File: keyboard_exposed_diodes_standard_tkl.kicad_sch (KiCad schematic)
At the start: 292 parts, among them J1 Conn_01x02_Male, J2 USB_C_Receptacle_USB2.0, SW1 Rotary_Encoder_Switch, U1 Pico

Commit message: Adding Net Names
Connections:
- net GND: now reaches C1.2, C10.2, C11.2, C12.2, C13.2, C14.2, C15.2, C16.2, C17.2, C18.2, C19.2, C2.2, C20.2, C21.2, C22.2, C23.2, C24.2, C25.2, C26.2, C27.2, C28.2, C29.2, C3.2, C30.2, C31.2, C32.2, C33.2, C34.2, C35.2, C36.2, C37.2, C38.2, C39.2, C4.2, C40.2, C41.2, C42.2, C43.2, C44.2, C45.2, C46.2, C47.2, C48.2, C49.2, C5.2, C50.2, C51.2, C52.2, C53.2, C54.2, C55.2, C56.2, C57.2, C58.2, C59.2, C6.2, C60.2, C61.2, C62.2, C63.2, C64.2, C65.2, C66.2, C67.2, C68.2, C69.2, C7.2, C70.2, C71.2, C72.2, C73.2, C74.2, C75.2, C76.2, C77.2, C78.2, C79.2, C8.2, C80.2, C81.2, C82.2, C83.2, C84.2, C85.2, C86.2, C87.2, C88.2, C89.2, C9.2, C90.2, C91.2, C92.2, C93.2, C94.2, C95.2, C96.1, D97.1 (GND), J2.A1 (GND), J2.A12 (GND), J2.B1 (GND), J2.B12 (GND), J2.S1 (SHIELD), SW1.C, U1.13 (GND), U1.18 (GND), U1.23 (GND), U1.28 (GND), U1.3 (GND), U1.38 (GND), U1.42 (GND), U1.8 (GND), U_0.1 (GND), U_1.1 (GND), U_2.1 (GND), U_3.1 (GND), U_4.1 (GND), U_5.1 (GND), U_6.1 (GND), U_7.1 (GND), U_8.1 (GND), U_9.1 (GND), U_A1.1 (GND), U_ACCENT1.1 (GND), U_B1.1 (GND), U_BKSPC1.1 (GND), U_BSLASH1.1 (GND), U_C1.1 (GND), U_CLOCK1.1 (GND), U_COMMA1.1 (GND), U_D1.1 (GND), U_DASH1.1 (GND), U_DEL1.1 (GND), U_DOWN1.1 (GND), U_E1.1 (GND), U_END1.1 (GND), U_ENT1.1 (GND), U_EQ1.1 (GND), U_ESC1.1 (GND), U_EX1.1 (GND), U_EX2.1 (GND), U_EX3.1 (GND), U_EX4.1 (GND), U_EX5.1 (GND), U_EX6.1 (GND), U_EX7.1 (GND), U_EX8.1 (GND), U_F1.1 (GND), U_F10.1 (GND), U_F11.1 (GND), U_F12.1 (GND), U_F13.1 (GND), U_F2.1 (GND), U_F3.1 (GND), U_F4.1 (GND), U_F5.1 (GND), U_F6.1 (GND), U_F7.1 (GND), U_F8.1 (GND), U_F9.1 (GND), U_FSLASH1.1 (GND), U_G1.1 (GND), U_H1.1 (GND), U_HOME1.1 (GND), U_I1.1 (GND), U_INSERT1.1 (GND), U_J1.1 (GND), U_K1.1 (GND), U_L1.1 (GND), U_LALT1.1 (GND), U_LBRACK1.1 (GND), U_LCTRL1.1 (GND), U_LEFT1.1 (GND), U_LSHIFT1.1 (GND), U_LSUPER1.1 (GND), U_M1.1 (GND), U_META1.1 (GND), U_N1.1 (GND), U_O1.1 (GND), U_P1.1 (GND), U_PAUSE1.1 (GND), U_PERIOD1.1 (GND), U_PGDN1.1 (GND), U_PGUP1.1 (GND), U_PRTSCR1.1 (GND), U_Q1.1 (GND), U_QUOTE1.1 (GND), U_R1.1 (GND), U_RALT1.1 (GND), U_RBRACK1.1 (GND), U_RCTRL1.1 (GND), U_RIGHT1.1 (GND), U_RSHIFT1.1 (GND), U_RSUPER1.1 (GND), U_S1.1 (GND), U_SCOL1.1 (GND), U_SLOC1.1 (GND), U_SPACE1.1 (GND), U_T1.1 (GND), U_TAB1.1 (GND), U_U1.1 (GND), U_UP1.1 (GND), U_V1.1 (GND), U_W1.1 (GND), U_X1.1 (GND), U_Y1.1 (GND), U_Z1.1 (GND)
- net COL 1: now reaches SW1.S2, U1.2 (GPIO1), U_1.5 (SW1), U_A1.5 (SW1), U_EX1.5 (SW1), U_LSUPER1.5 (SW1), U_Q1.5 (SW1), U_Z1.5 (SW1)
- net PWR: now reaches C1.1, C10.1, C11.1, C12.1, C13.1, C14.1, C15.1, C16.1, C17.1, C18.1, C19.1, C2.1, C20.1, C21.1, C22.1, C23.1, C24.1, C25.1, C26.1, C27.1, C28.1, C29.1, C3.1, C30.1, C31.1, C32.1, C33.1, C34.1, C35.1, C36.1, C37.1, C38.1, C39.1, C4.1, C40.1, C41.1, C42.1, C43.1, C44.1, C45.1, C46.1, C47.1, C48.1, C49.1, C5.1, C50.1, C51.1, C52.1, C53.1, C54.1, C55.1, C56.1, C57.1, C58.1, C59.1, C6.1, C60.1, C61.1, C62.1, C63.1, C64.1, C65.1, C66.1, C67.1, C68.1, C69.1, C7.1, C70.1, C71.1, C72.1, C73.1, C74.1, C75.1, C76.1, C77.1, C78.1, C79.1, C8.1, C80.1, C81.1, C82.1, C83.1, C84.1, C85.1, C86.1, C87.1, C88.1, C89.1, C9.1, C90.1, C91.1, C92.1, C93.1, C94.1, C95.1, D96.2 (A), J2.A4 (VBUS), J2.A9 (VBUS), J2.B4 (VBUS), J2.B9 (VBUS), U1.40 (VBUS), U_0.4 (VCC), U_1.4 (VCC), U_2.4 (VCC), U_3.4 (VCC), U_4.4 (VCC), U_5.4 (VCC), U_6.4 (VCC), U_7.4 (VCC), U_8.4 (VCC), U_9.4 (VCC), U_A1.4 (VCC), U_ACCENT1.4 (VCC), U_B1.4 (VCC), U_BKSPC1.4 (VCC), U_BSLASH1.4 (VCC), U_C1.4 (VCC), U_CLOCK1.4 (VCC), U_COMMA1.4 (VCC), U_D1.4 (VCC), U_DASH1.4 (VCC), U_DEL1.4 (VCC), U_DOWN1.4 (VCC), U_E1.4 (VCC), U_END1.4 (VCC), U_ENT1.4 (VCC), U_EQ1.4 (VCC), U_ESC1.4 (VCC), U_EX1.4 (VCC), U_EX2.4 (VCC), U_EX3.4 (VCC), U_EX4.4 (VCC), U_EX5.4 (VCC), U_EX6.4 (VCC), U_EX7.4 (VCC), U_EX8.4 (VCC), U_F1.4 (VCC), U_F10.4 (VCC), U_F11.4 (VCC), U_F12.4 (VCC), U_F13.4 (VCC), U_F2.4 (VCC), U_F3.4 (VCC), U_F4.4 (VCC), U_F5.4 (VCC), U_F6.4 (VCC), U_F7.4 (VCC), U_F8.4 (VCC), U_F9.4 (VCC), U_FSLASH1.4 (VCC), U_G1.4 (VCC), U_H1.4 (VCC), U_HOME1.4 (VCC), U_I1.4 (VCC), U_INSERT1.4 (VCC), U_J1.4 (VCC), U_K1.4 (VCC), U_L1.4 (VCC), U_LALT1.4 (VCC), U_LBRACK1.4 (VCC), U_LCTRL1.4 (VCC), U_LEFT1.4 (VCC), U_LSHIFT1.4 (VCC), U_LSUPER1.4 (VCC), U_M1.4 (VCC), U_META1.4 (VCC), U_N1.4 (VCC), U_O1.4 (VCC), U_P1.4 (VCC), U_PAUSE1.4 (VCC), U_PERIOD1.4 (VCC), U_PGDN1.4 (VCC), U_PGUP1.4 (VCC), U_PRTSCR1.4 (VCC), U_Q1.4 (VCC), U_QUOTE1.4 (VCC), U_R1.4 (VCC), U_RALT1.4 (VCC), U_RBRACK1.4 (VCC), U_RCTRL1.4 (VCC), U_RIGHT1.4 (VCC), U_RSHIFT1.4 (VCC), U_RSUPER1.4 (VCC), U_S1.4 (VCC), U_SCOL1.4 (VCC), U_SLOC1.4 (VCC), U_SPACE1.4 (VCC), U_T1.4 (VCC), U_TAB1.4 (VCC), U_U1.4 (VCC), U_UP1.4 (VCC), U_V1.4 (VCC), U_W1.4 (VCC), U_X1.4 (VCC), U_Y1.4 (VCC), U_Z1.4 (VCC)
- net ROW 0: now reaches D_ESC1.1 (K), D_EX1.1 (K), D_F1.1 (K), D_F10.1 (K), D_F11.1 (K), D_F12.1 (K), D_F2.1 (K), D_F3.1 (K), D_F4.1 (K), D_F5.1 (K), D_F6.1 (K), D_F7.1 (K), D_F8.1 (K), D_F9.1 (K), D_PAUSE1.1 (K), D_PRTSCR1.1 (K), D_SLOC1.1 (K), U1.22 (GPIO17)
- net COL 0: now reaches U1.1 (GPIO0), U_ACCENT1.5 (SW1), U_CLOCK1.5 (SW1), U_ESC1.5 (SW1), U_LCTRL1.5 (SW1), U_LSHIFT1.5 (SW1), U_TAB1.5 (SW1)
- net COL 2: now reaches U1.4 (GPIO2), U_2.5 (SW1), U_F1.5 (SW1), U_LALT1.5 (SW1), U_S1.5 (SW1), U_W1.5 (SW1), U_X1.5 (SW1)
- net COL 3: now reaches U1.5 (GPIO3), U_3.5 (SW1), U_C1.5 (SW1), U_D1.5 (SW1), U_E1.5 (SW1), U_F2.5 (SW1)
- net COL 4: now reaches U1.6 (GPIO4), U_4.5 (SW1), U_EX2.5 (SW1), U_F13.5 (SW1), U_F3.5 (SW1), U_R1.5 (SW1), U_V1.5 (SW1)
- net COL 5: now reaches U1.7 (GPIO5), U_5.5 (SW1), U_B1.5 (SW1), U_F4.5 (SW1), U_G1.5 (SW1), U_SPACE1.5 (SW1), U_T1.5 (SW1)
- net COL 6: now reaches U1.9 (GPIO6), U_6.5 (SW1), U_EX3.5 (SW1), U_F5.5 (SW1), U_H1.5 (SW1), U_N1.5 (SW1), U_Y1.5 (SW1)
- net COL 7: now reaches U1.10 (GPIO7), U_7.5 (SW1), U_F6.5 (SW1), U_J1.5 (SW1), U_M1.5 (SW1), U_U1.5 (SW1)
- net COL 8: now reaches U1.11 (GPIO8), U_8.5 (SW1), U_COMMA1.5 (SW1), U_F7.5 (SW1), U_I1.5 (SW1), U_K1.5 (SW1)
- net COL 9: now reaches U1.12 (GPIO9), U_9.5 (SW1), U_F8.5 (SW1), U_L1.5 (SW1), U_O1.5 (SW1), U_PERIOD1.5 (SW1), U_RALT1.5 (SW1)
- net COL 10: now reaches U1.14 (GPIO10), U_0.5 (SW1), U_F9.5 (SW1), U_FSLASH1.5 (SW1), U_P1.5 (SW1), U_RSUPER1.5 (SW1), U_SCOL1.5 (SW1)
- net COL 11: now reaches U1.15 (GPIO11), U_DASH1.5 (SW1), U_F10.5 (SW1), U_LBRACK1.5 (SW1), U_META1.5 (SW1), U_QUOTE1.5 (SW1)
- net COL 12: now reaches U1.16 (GPIO12), U_EQ1.5 (SW1), U_F11.5 (SW1), U_RBRACK1.5 (SW1)
- net COL 13: now reaches U1.17 (GPIO13), U_BKSPC1.5 (SW1), U_BSLASH1.5 (SW1), U_ENT1.5 (SW1), U_F12.5 (SW1), U_RCTRL1.5 (SW1), U_RSHIFT1.5 (SW1)
- net COL 14: now reaches U1.19 (GPIO14), U_DEL1.5 (SW1), U_EX4.5 (SW1), U_EX5.5 (SW1), U_INSERT1.5 (SW1), U_LEFT1.5 (SW1), U_PRTSCR1.5 (SW1)
- net COL 15: now reaches U1.20 (GPIO15), U_DOWN1.5 (SW1), U_END1.5 (SW1), U_EX6.5 (SW1), U_HOME1.5 (SW1), U_SLOC1.5 (SW1), U_UP1.5 (SW1)
- net COL 16: now reaches U1.21 (GPIO16), U_EX7.5 (SW1), U_EX8.5 (SW1), U_PAUSE1.5 (SW1), U_PGDN1.5 (SW1), U_PGUP1.5 (SW1), U_RIGHT1.5 (SW1)
- net ROW 1: now reaches D_0.1 (K), D_1.1 (K), D_2.1 (K), D_3.1 (K), D_4.1 (K), D_5.1 (K), D_6.1 (K), D_7.1 (K), D_8.1 (K), D_9.1 (K), D_ACCENT1.1 (K), D_BKSPC1.1 (K), D_DASH1.1 (K), D_EQ1.1 (K), D_HOME1.1 (K), D_INSERT1.1 (K), D_PGUP1.1 (K), U1.25 (GPIO19)
- net ROW 2: now reaches D_BSLASH1.1 (K), D_DEL1.1 (K), D_E1.1 (K), D_END1.1 (K), D_I1.1 (K), D_LBRACK1.1 (K), D_O1.1 (K), D_P1.1 (K), D_PGDN1.1 (K), D_Q1.1 (K), D_R1.1 (K), D_RBRACK1.1 (K), D_T1.1 (K), D_TAB1.1 (K), D_U1.1 (K), D_W1.1 (K), D_Y1.1 (K), U1.26 (GPIO20)
- net ROW 3: now reaches D_A1.1 (K), D_CLOCK1.1 (K), D_D1.1 (K), D_ENT1.1 (K), D_EX4.1 (K), D_EX6.1 (K), D_EX7.1 (K), D_F13.1 (K), D_G1.1 (K), D_H1.1 (K), D_J1.1 (K), D_K1.1 (K), D_L1.1 (K), D_QUOTE1.1 (K), D_S1.1 (K), D_SCOL1.1 (K), U1.27 (GPIO21)
- net ROW 4: now reaches D_B1.1 (K), D_C1.1 (K), D_COMMA1.1 (K), D_EX5.1 (K), D_EX8.1 (K), D_FSLASH1.1 (K), D_LSHIFT1.1 (K), D_M1.1 (K), D_N1.1 (K), D_PERIOD1.1 (K), D_RSHIFT1.1 (K), D_UP1.1 (K), D_V1.1 (K), D_X1.1 (K), D_Z1.1 (K), U1.29 (GPIO22)
- net ROW 5: now reaches D_DOWN1.1 (K), D_EX2.1 (K), D_EX3.1 (K), D_LALT1.1 (K), D_LCRTL1.1 (K), D_LEFT1.1 (K), D_LSUPER1.1 (K), D_META1.1 (K), D_RALT1.1 (K), D_RCTRL1.1 (K), D_RIGHT1.1 (K), D_RSUPER1.1 (K), D_SPACE1.1 (K), U1.31 (GPIO26_ADC0)
- no-connect marks 10 -> 13

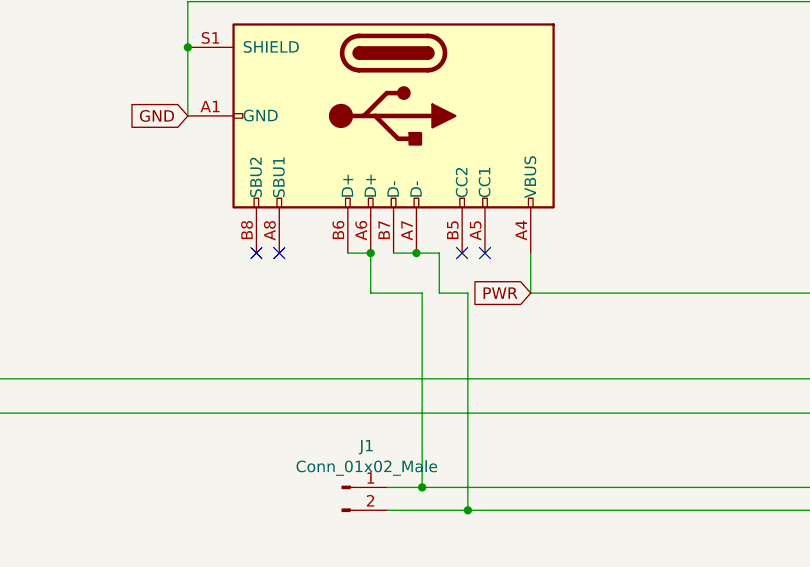
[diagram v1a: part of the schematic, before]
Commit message: REduce PCB Spacing to match jlcpcb minimum. Redo USB C data traces
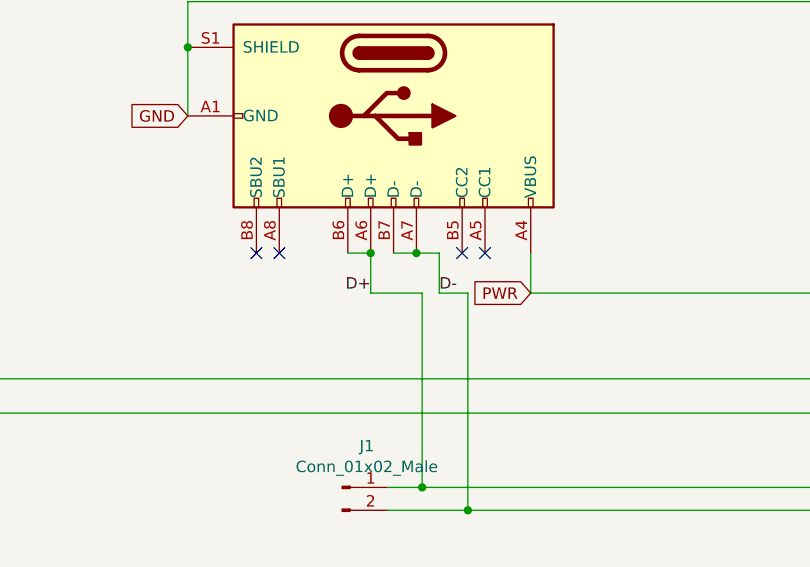
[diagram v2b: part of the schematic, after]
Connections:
- net D+: now reaches J1.1 (Pin_1), J2.A6 (D+), J2.B6 (D+), U1.44 (D+)
- net D-: now reaches J1.2 (Pin_2), J2.A7 (D-), J2.B7 (D-), U1.45 (D-)
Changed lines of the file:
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@@
+    (effects (font (size 1.27 1.27)) (justify left bottom))
+  )
+  (label "D-" (at 454.025 158.75 0)
     (effects (font (size 1.27 1.27)) (justify left bottom))
   )
@@
     (effects (font (size 1.27 1.27)) (justify left bottom))
   )
+  (label "D+" (at 446.405 158.75 180)
+    (effects (font (size 1.27 1.27)) (justify right bottom))
+  )
   (global_label "PWR" (shape input) (at 464.185 158.75 180) (fields_autoplaced)

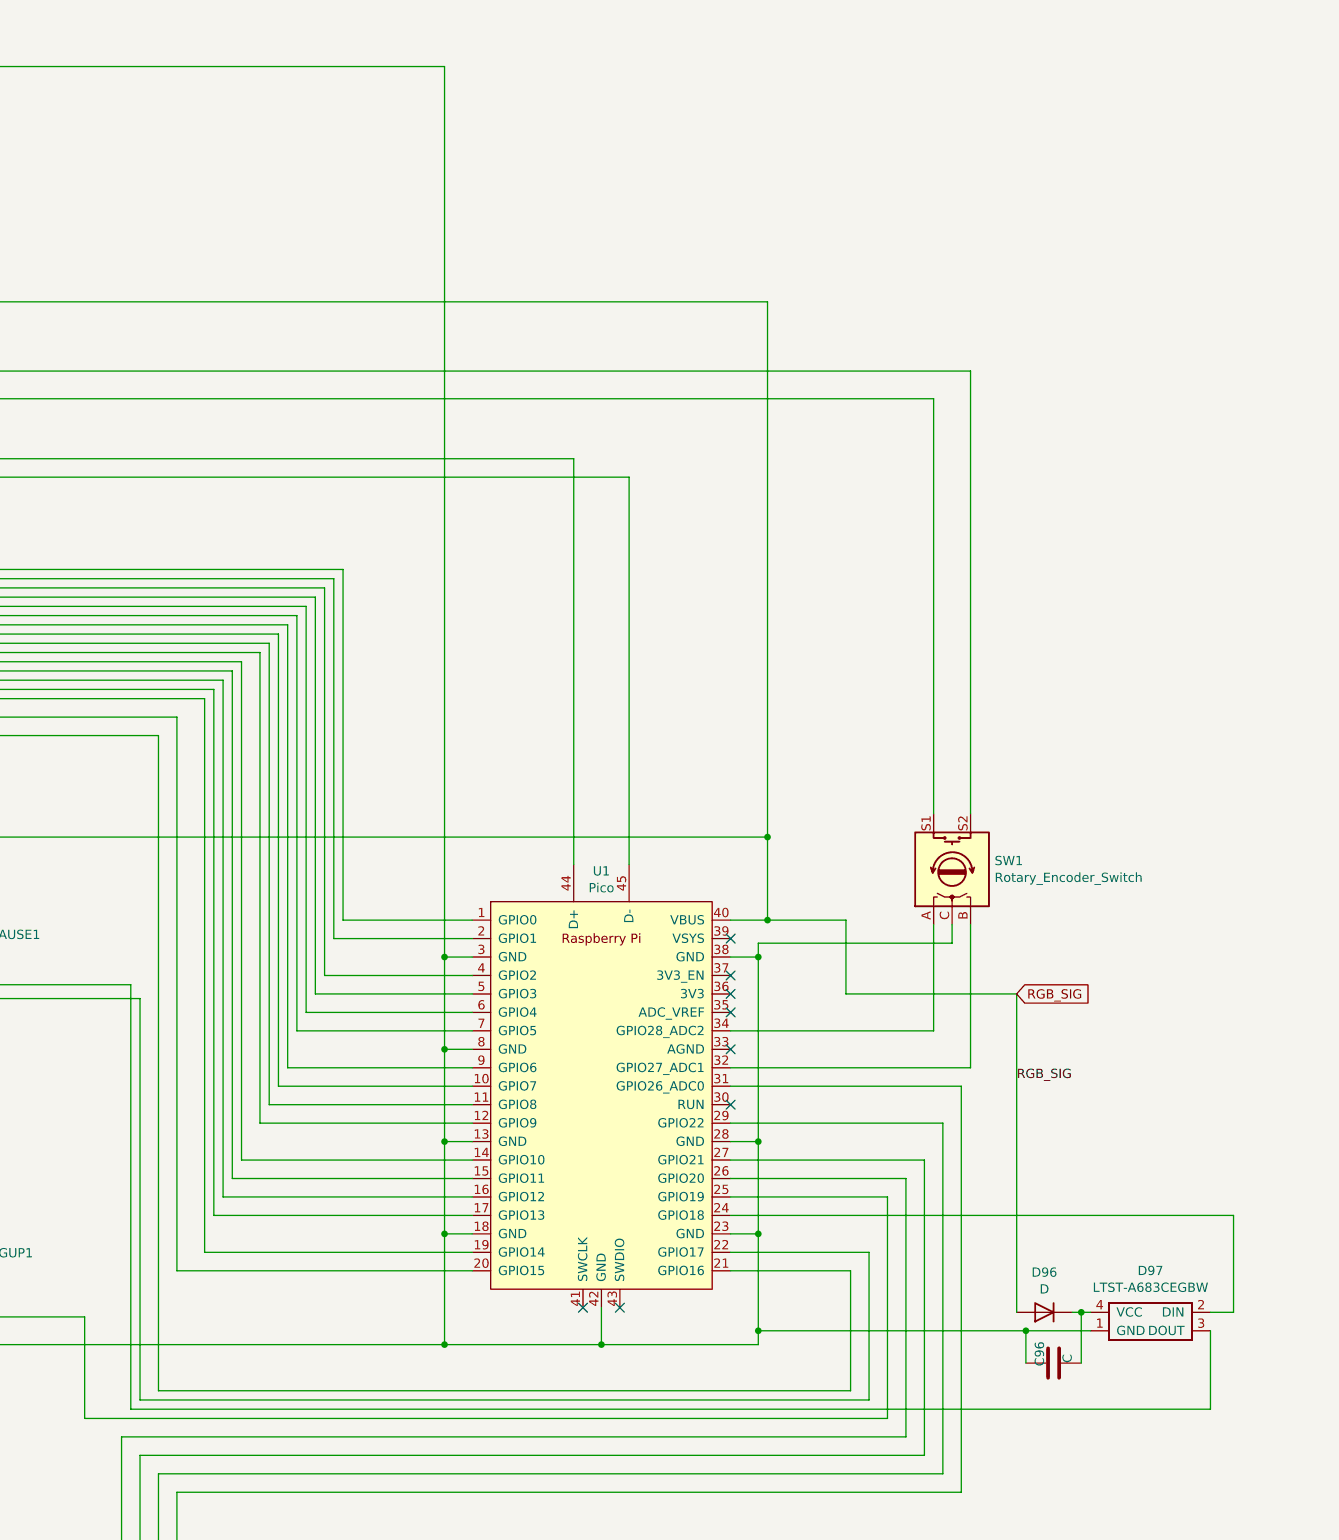
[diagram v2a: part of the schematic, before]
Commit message: Remove step up led. Use gate instead
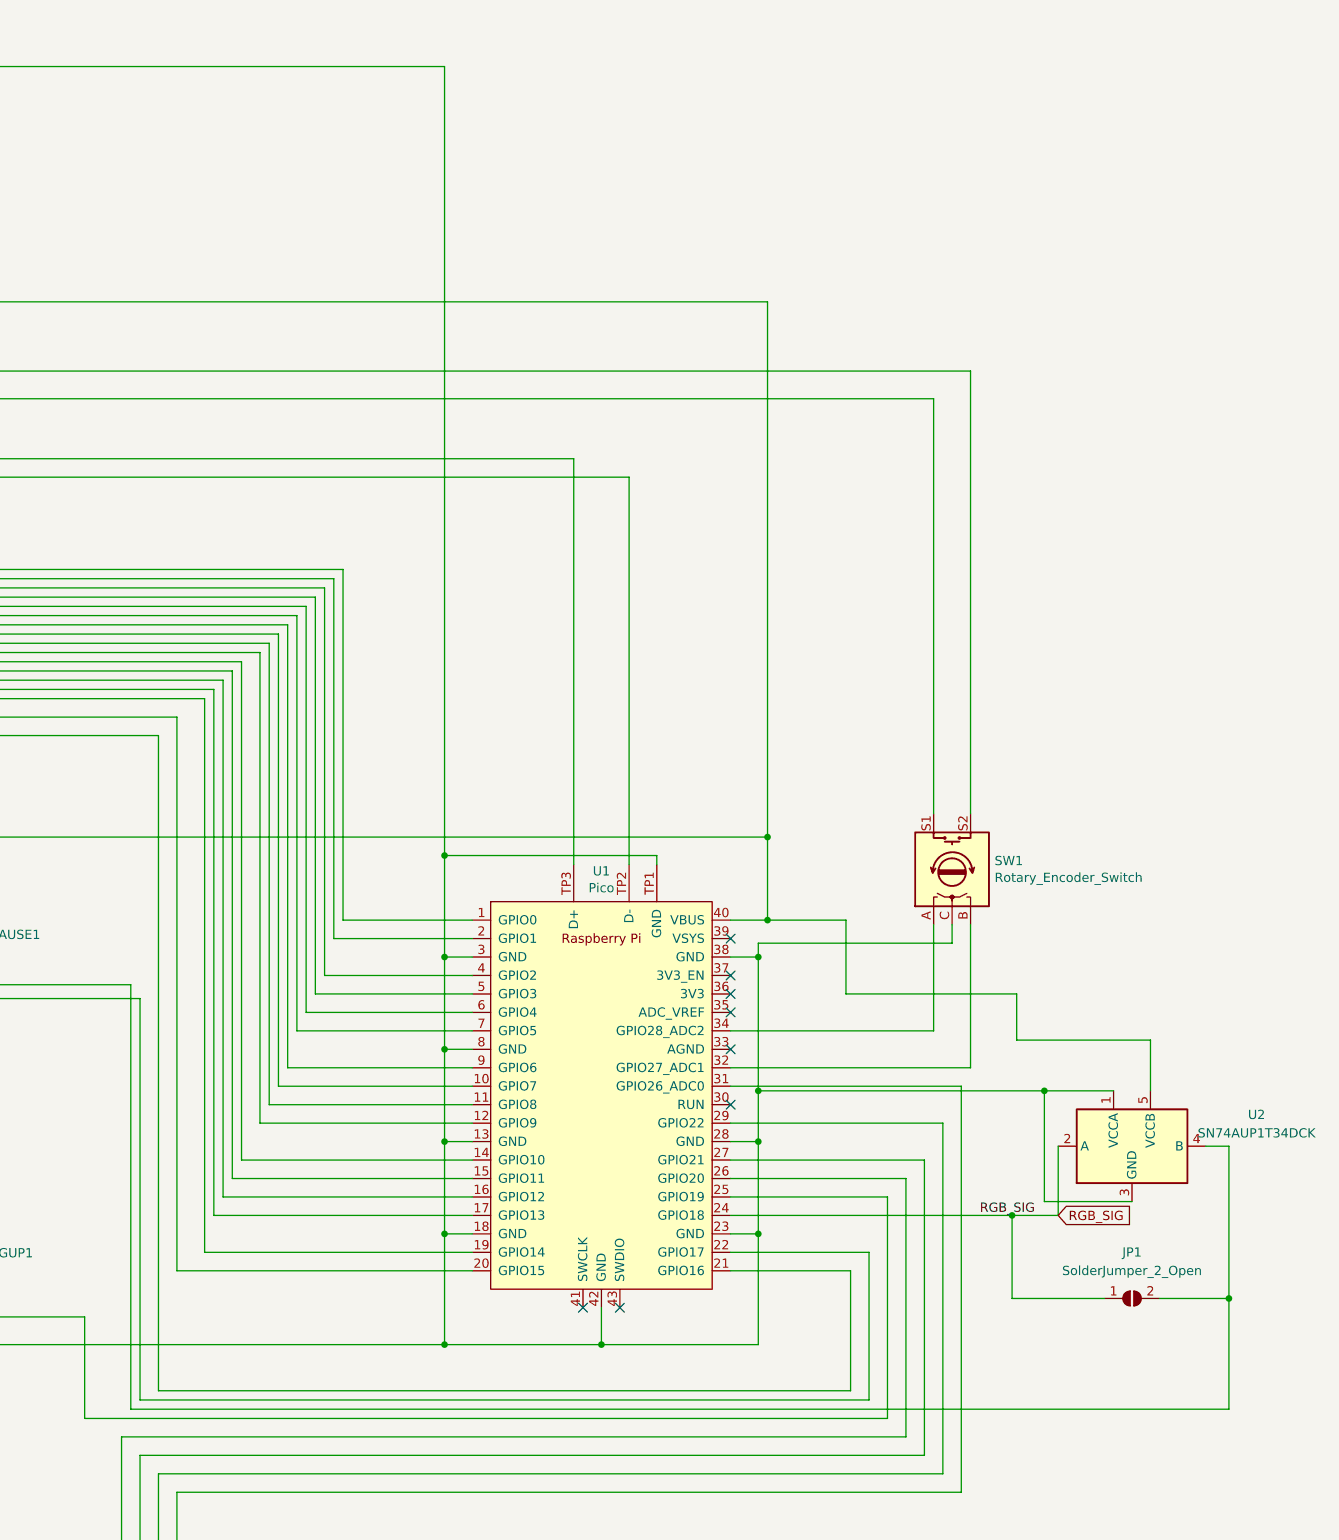
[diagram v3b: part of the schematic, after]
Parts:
- removed C96: C, Capacitor_SMD:C_0805_2012Metric, symbol Device:C
- removed D96: D, Diode_THT:D_DO-35_SOD27_P7.62mm_Horizontal, symbol Device:D
- removed D97: LTST-A683CEGBW, Cherry MX:LTST-A683CEGBW, symbol Cherry_MX:LTST-A683CEGBW
- added JP1: SolderJumper_2_Open, Jumper:SolderJumper-2_P1.3mm_Open_RoundedPad1.0x1.5mm, symbol Jumper:SolderJumper_2_Open
- added U2: SN74AUP1T34DCK, Package_TO_SOT_SMD:SOT-353_SC-70-5, symbol Logic_LevelTranslator:SN74AUP1T34DCK
- U1: footprint MCU_RaspberryPi_and_Boards:RPi_Pico_SMD_TH_usb_tp -> MCU_RaspberryPi_and_Boards:RPi_Pico_SMD_TH
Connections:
- net D+: now also U1.TP3 (D+); no longer U1.44 (D+)
- net D-: now also U1.TP2 (D-); no longer U1.45 (D-)
- net GND: now also U1.TP1 (GND), U2.1 (VCCA), U2.3 (GND)
- net PWR: now also U2.5 (VCCB)
- net at U_PAUSE1.2 (DIN): now also JP1.2 (B), U2.4 (B)
- net RGB_SIG: now reaches U1.24 (GPIO18)
- net RGB_SIG: now also JP1.1 (A), U2.2 (A)

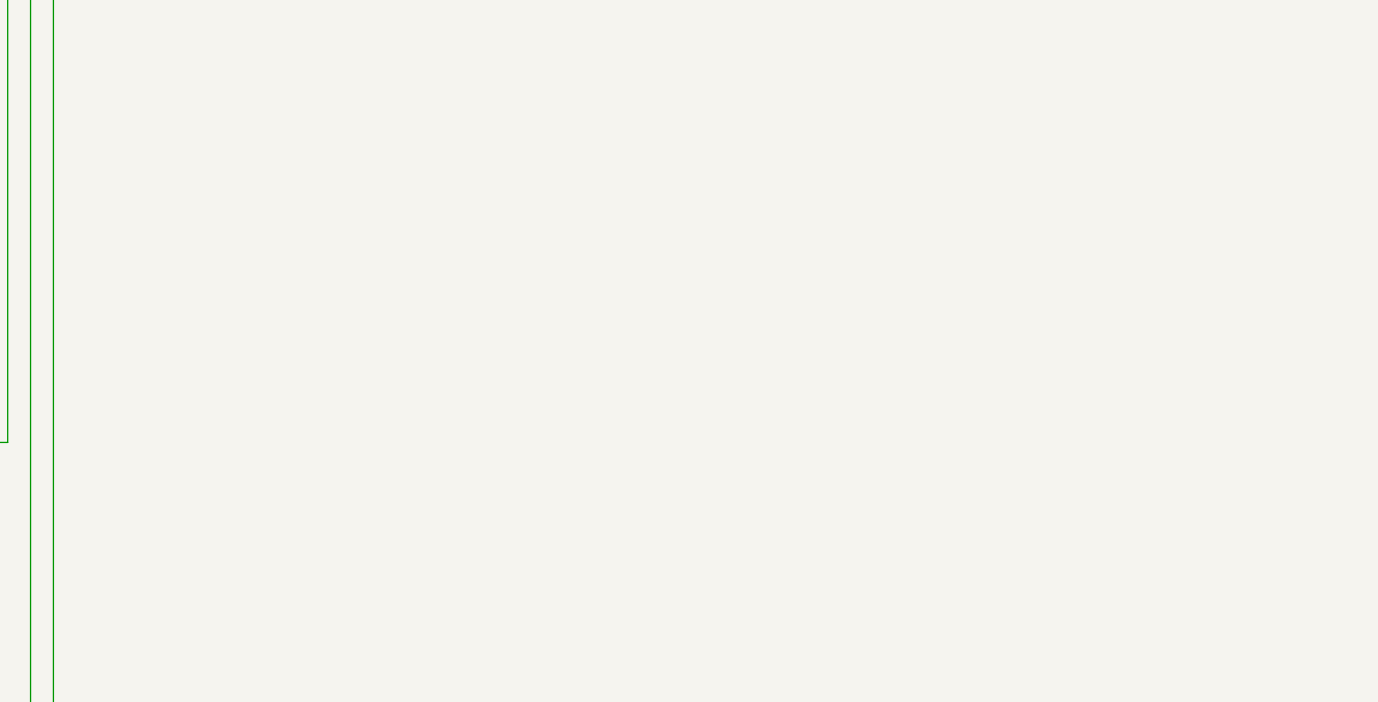
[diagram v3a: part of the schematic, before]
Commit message: Incude mount holes and stabilizer holes in schematic
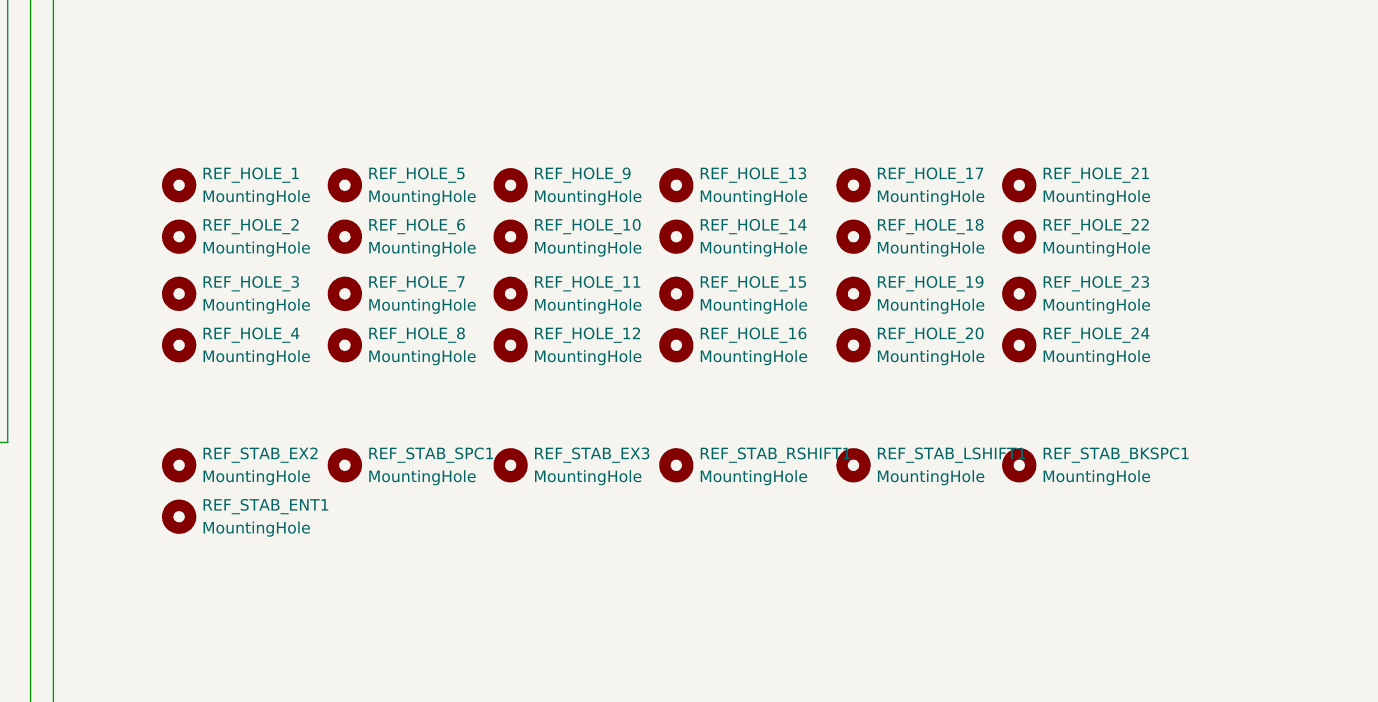
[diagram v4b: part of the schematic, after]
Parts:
- added REF_HOLE_1, REF_HOLE_10, REF_HOLE_11, REF_HOLE_12, REF_HOLE_13, REF_HOLE_14, REF_HOLE_15, REF_HOLE_16, REF_HOLE_17, REF_HOLE_18, REF_HOLE_19, REF_HOLE_2, REF_HOLE_20, REF_HOLE_21, REF_HOLE_22, REF_HOLE_23, REF_HOLE_24, REF_HOLE_3, REF_HOLE_4, REF_HOLE_5, REF_HOLE_6, REF_HOLE_7, REF_HOLE_8, REF_HOLE_9: MountingHole, MountingHole:MountingHole_4.3mm_M4, symbol Mechanical:MountingHole
- added REF_STAB_BKSPC1, REF_STAB_ENT1, REF_STAB_EX2, REF_STAB_EX3, REF_STAB_LSHIFT1, REF_STAB_RSHIFT1, REF_STAB_SPC1: MountingHole, Mounting_Keyboard_Stabilizer:Stabilizer_Cherry_MX_2u, symbol Mechanical:MountingHole
